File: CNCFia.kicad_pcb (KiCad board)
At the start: 2 copper layers, 128.3 x 96.5 mm, 89 parts, among them J1 GND, J10 Driver_X, J11 Driver_Y, J12 Driver_Z, J14 Spin_10V, J15 Relay_1, J16 Relay_2, J17 Relay_3, J2 EXT_5V, J3 Limit SW_XY, J4 Limit SW_ZA, J5 Extra SW 0, J6 Extra SW 1, J7 EXT_12V, J8 OPTO_5V, J9 Signal Input, Q1 BSS138, Q13 2N3904, Q14 2N3904, Q15 2N3904, Q2 BSS138, Q3 BSS138, Q4 BSS138, Q5 BSS138, Q6 BSS138, Q7 BSS138, Q8 BSS138, Q9 BSS138, U1 LTV-847, U2 LTV-847, U5 LM358P

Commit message: Before autorouting
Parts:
- renumbered REF** to M3-1, REF** to M3-2, REF** to M3-3, REF** to M3-4
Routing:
- net OPTO_5V: track 143.4 -> 142.4 mm

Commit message: Pre-SMD
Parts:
- moved M3-2 19.2 mm to (52.1, 100.2)
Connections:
- net LV_1 renamed X_Enbl
- net LV_2 renamed X_Dir
- net LV_3 renamed X_Step
- net LV_4 renamed Y_Enbl
- net LV_5 renamed Y_Dir
- net LV_6 renamed Y_Step
- net LV_7 renamed Z_Enbl
- net LV_8 renamed Z_Dir
- net LV_9 renamed Z_Step
- J1 pad 2: GND -> +5V
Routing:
- net GND: track 69.0 -> 195.1 mm, vias 1 -> 0
- net +5V: track 152.4 -> 235.4 mm
- net Probe: track 119.0 -> 53.7 mm
- net LIM_YMin: track 118.2 -> 63.8 mm
- net IN_Relay_1: track 112.0 -> 59.6 mm
- net Z_Dir: track 157.8 -> 105.8 mm, vias 1 -> 0
- net IN_Relay_2: track 120.5 -> 70.5 mm
- net Net-(D5-Pad2): track 136.1 -> 86.5 mm
- net Z_Step: track 157.0 -> 110.7 mm
- net X_Step: track 125.9 -> 82.0 mm, vias 0 -> 1
- net LIM_YMax: track 118.4 -> 75.2 mm
- net LIM_ZMax: track 95.9 -> 55.0 mm
- net Y_Dir: track 130.4 -> 90.2 mm, vias 1 -> 0
- net IN_Relay_3: track 117.4 -> 82.5 mm
- net LIM_XMax: track 93.6 -> 59.6 mm
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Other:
- board text added: "+12V GND"
- board text added: "+5V GND"
- board text added: "+5V OUT GND"
- board text added: "5V Source"
- board text added: "Controller Input"
- board text added: "Extra Probe Z Max Z Min"
- board text added: "GND E. Stop C. Start"
- board text added: "GND F. Hold Reset Door"
- board text added: "GND Spindle 0-10V"
- board text added: "NO COM NC Relay 2"
- board text added: "NO COM NC Relay 3"
- board text added: "Opto 5V GND"
- board text added: "Opto V Source"
- board text added: "X Step Dir Enable"
- board text added: "Y Max Y Min X Max X Min"
- board text added: "Y Step Dir Enable"
- board text added: "Z Step Dir Enable"
- board text added: "c6p.dev CNCFia b1"

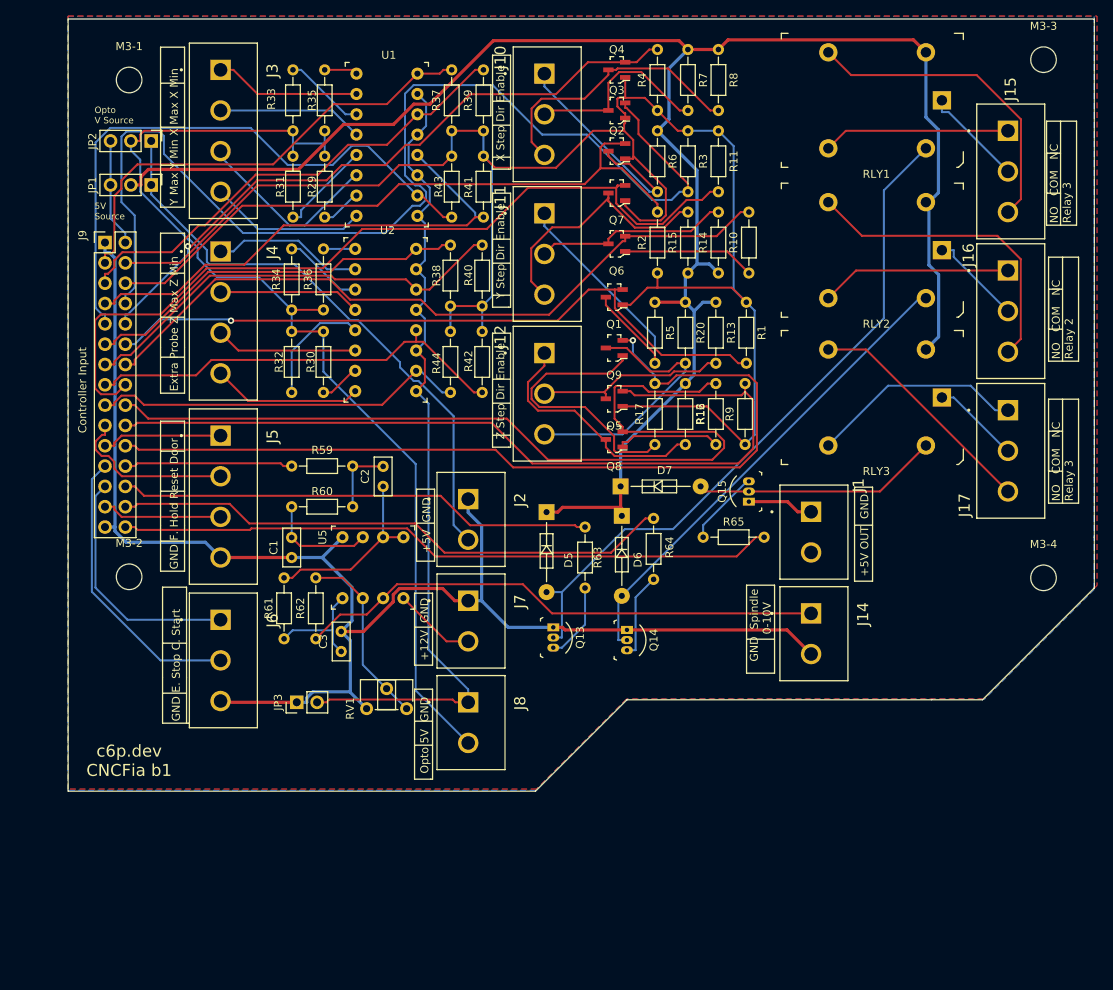
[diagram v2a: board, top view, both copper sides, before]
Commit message: Makes it SMD based, with smaller connectors
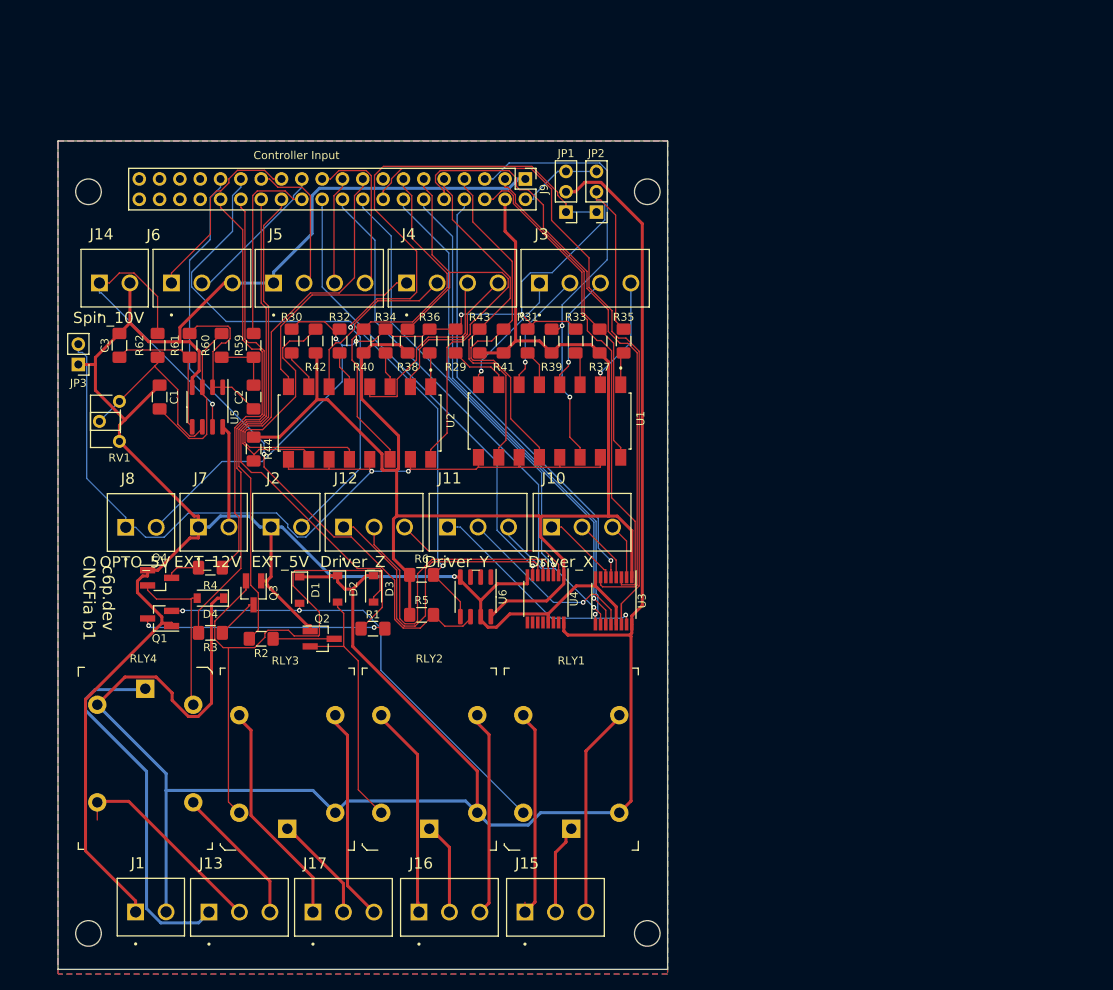
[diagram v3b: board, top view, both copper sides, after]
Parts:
- removed M3-1, M3-2, M3-3, M3-4: MountingHole_3.2mm_M3, MountingHole:MountingHole_3.2mm_M3
- removed Q13, Q14: 2N3904, digikey-footprints:TO-92-3
- removed the Q3 at (113.0, 41.9)
- removed Q5, Q6, Q7, Q8, Q9: BSS138, digikey-footprints:SOT-23-3
- removed R10, R11, R12, R13, R14, R15, R16, R17, R20, R7, R8, R9: 10k, Resistor_THT:R_Axial_DIN0204_L3.6mm_D1.6mm_P7.62mm_Horizontal
- removed R63, R64, R65: 2k2, Resistor_THT:R_Axial_DIN0204_L3.6mm_D1.6mm_P7.62mm_Horizontal
- added D4: 1N4148, Diode_SMD:D_SOD-123, F.Cu at (62.2, 102.9)
- added J13: Coolant, Kicad_extra_components:CUI_TBP02R2-381-03BE, F.Cu at (62.0, 142.1)
- added MH1: MountingHole_3.2mm_M3, MountingHole:MountingHole_3.2mm_M3, F.Cu at (116.8, 52.1)
- added MH2: MountingHole_3.2mm_M3, MountingHole:MountingHole_3.2mm_M3, F.Cu at (116.8, 144.8)
- added MH3: MountingHole_3.2mm_M3, MountingHole:MountingHole_3.2mm_M3, F.Cu at (47.0, 144.8)
- added MH4: MountingHole_3.2mm_M3, MountingHole:MountingHole_3.2mm_M3, F.Cu at (47.0, 52.1)
- added RLY4: G5LE-14_DC5, digikey-footprints:Relay_THT_G5LE-14, F.Cu at (54.1, 114.2)
- added U3: 4504, Package_SO:TSSOP-16_4.4x5mm_P0.65mm, F.Cu at (112.6, 103.2)
- added U4: 4504, Package_SO:TSSOP-16_4.4x5mm_P0.65mm, F.Cu at (104.1, 103.0)
- added U6: 24LC16, Package_SO:SOIC-8_3.9x4.9mm_P1.27mm, F.Cu at (95.4, 102.7)
- C1, C2, C3: footprint Kicad_extra_components:C_Rect_L4.6mm_W2.0mm_P2.50mm_MKS02_FKP02 -> Capacitor_SMD:C_1206_3216Metric_Pad1.42x1.75mm_HandSolder
- D1: renamed from D5; footprint digikey-footprints:Diode_DO-35_P10mm -> Diode_SMD:D_SOD-123
- D2: renamed from D6; footprint digikey-footprints:Diode_DO-35_P10mm -> Diode_SMD:D_SOD-123
- D3: renamed from D7; footprint digikey-footprints:Diode_DO-35_P10mm -> Diode_SMD:D_SOD-123
- J1, J14, J2, J7, J8: footprint Kicad_extra_components:CUI_TBP01R2-508-02BE -> Kicad_extra_components:CUI_TBP02R2-381-02BE
- J10, J11, J12, J6: footprint Kicad_extra_components:CUI_TBP01R2-508-03BE -> Kicad_extra_components:CUI_TBP02R2-381-03BE
- J15: value Relay_1 -> Spin_Enabl; footprint Kicad_extra_components:CUI_TBP01R2-508-03BE -> Kicad_extra_components:CUI_TBP02R2-381-03BE
- J16: value Relay_2 -> Spin_Dir; footprint Kicad_extra_components:CUI_TBP01R2-508-03BE -> Kicad_extra_components:CUI_TBP02R2-381-03BE
- J17: value Relay_3 -> Mist; footprint Kicad_extra_components:CUI_TBP01R2-508-03BE -> Kicad_extra_components:CUI_TBP02R2-381-03BE
- J3, J4, J5: footprint Kicad_extra_components:CUI_TBP01R2-508-04BE -> Kicad_extra_components:CUI_TBP02R2-381-04BE
- J9: footprint Connector_PinHeader_2.54mm:PinHeader_2x15_P2.54mm_Vertical -> Connector_PinHeader_2.54mm:PinHeader_2x20_P2.54mm_Vertical
- Q1, Q2, Q4: value BSS138 -> 2N3904; footprint digikey-footprints:SOT-23-3 -> Package_TO_SOT_SMD:SOT-23_Handsoldering
- Q3: renamed from Q15; footprint digikey-footprints:TO-92-3 -> Package_TO_SOT_SMD:SOT-23_Handsoldering
- R1, R2, R3, R4, R5, R6: value 10k -> 2k2; footprint Resistor_THT:R_Axial_DIN0204_L3.6mm_D1.6mm_P7.62mm_Horizontal -> Resistor_SMD:R_1206_3216Metric_Pad1.42x1.75mm_HandSolder
- R29, R30, R31, R32, R33, R34, R35, R36, R37, R38, R39, R40, R41, R42, R43, R44, R59, R60, R61, R62: footprint Resistor_THT:R_Axial_DIN0204_L3.6mm_D1.6mm_P7.62mm_Horizontal -> Resistor_SMD:R_1206_3216Metric_Pad1.42x1.75mm_HandSolder
- U1, U2: footprint digikey-footprints:Socket_DIP-16_7.62mm_Conn -> Kicad_extra_components:SOIC254P1016X460-16N
- U5: footprint digikey-footprints:SOCKET_DIP-8_7.62mm_Conn -> Package_SO:SOIC-8_3.9x4.9mm_P1.27mm
- moved J15 114.8 mm to (101.5, 142.1), turned to 0 degrees
- moved J16 108.9 mm to (88.3, 142.1), turned to 0 degrees
- moved J17 107.2 mm to (75.0, 142.1), turned to 0 degrees
- moved RLY1 102.2 mm to (107.3, 131.7), turned to 90 degrees
- moved J1 98.1 mm to (52.9, 142.1), turned to 0 degrees
- moved J14 98.1 mm to (48.4, 63.5), turned to 0 degrees
- moved RLY3 98.0 mm to (71.8, 131.7), turned to 90 degrees
- moved RLY2 96.6 mm to (89.6, 131.7), turned to 90 degrees
- moved R3 86.6 mm to (62.2, 107.2), turned to 180 degrees
- moved Q4 85.4 mm to (55.9, 100.3), turned to 0 degrees
- moved R4 79.9 mm to (62.2, 99.1), turned to 0 degrees
- moved Q2 71.2 mm to (76.2, 108.0), turned to 0 degrees
- moved Q1 69.6 mm to (55.9, 105.4)
- moved R2 67.4 mm to (68.6, 108.0), turned to 180 degrees
- moved Q3 63.0 mm to (67.6, 102.2), turned to -90 degrees
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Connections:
- net /PWM to V converter/OUT_Spn_10V_0 renamed /OUT_Spn_10V_0
- net /Relays/Relay_COM_1 renamed /Relay_COM_1
- net /Relays/Relay_COM_2 renamed /Relay_COM_2
- net /Relays/Relay_COM_3 renamed /Relay_COM_3
- net /Relays/Relay_NC_1 renamed /Relay_NC_1
- net /Relays/Relay_NC_2 renamed /Relay_NC_2
- net /Relays/Relay_NC_3 renamed /Relay_NC_3
- net /Relays/Relay_NO_1 renamed /Relay_NO_1
- net /Relays/Relay_NO_2 renamed /Relay_NO_2
- net /Relays/Relay_NO_3 renamed /Relay_NO_3
- net SPIN_PWM renamed Spin_PWM
- D1 pad 2: Net-(D5-Pad2) -> Net-(D1-Pad2)
- D2 pad 2: Net-(D6-Pad2) -> Net-(D2-Pad2)
- J10 pad 1: /Level Shifters/HV_1 -> /HV_3
- J10 pad 2: /Level Shifters/HV_2 -> /HV_2
- J10 pad 3: /Level Shifters/HV_3 -> /HV_1
- J11 pad 1: /Level Shifters/HV_4 -> /HV_6
- J11 pad 2: /Level Shifters/HV_5 -> /HV_5
- J11 pad 3: /Level Shifters/HV_6 -> /HV_4
- J12 pad 1: /Level Shifters/HV_7 -> /HV_9
- J12 pad 2: /Level Shifters/HV_8 -> /HV_8
- J12 pad 3: /Level Shifters/HV_9 -> /HV_7
- J3 pad 1: /Opto-isolated switches/SW_XMIN -> /SW_YMAX
- J3 pad 2: /Opto-isolated switches/SW_XMAX -> /SW_YMIN
- J3 pad 3: /Opto-isolated switches/SW_YMIN -> /SW_XMAX
- J3 pad 4: /Opto-isolated switches/SW_YMAX -> /SW_XMIN
- J4 pad 1: /Opto-isolated switches/SW_ZMIN -> /SW_Extra
- J4 pad 2: /Opto-isolated switches/SW_ZMAX -> /SW_Probe
- J4 pad 3: /Opto-isolated switches/SW_Probe -> /SW_ZMAX
- J4 pad 4: /Opto-isolated switches/SW_Extra -> /SW_ZMIN
- J5 pad 1: Door -> GND
- J5 pad 2: Reset -> Feed_Hold
- J5 pad 3: Feed_Hold -> Reset
- J5 pad 4: GND -> Door
- J9 pad 26: IN_Relay_1 -> Spin_Enbl
- J9 pad 28: IN_Relay_2 -> Spin_Dir
- J9 pad 29: GND -> E_SDA
- J9 pad 30: IN_Relay_3 -> Mist
- Q1 pad 1: +3V3 -> GND
- Q1 pad 2: Y_Enbl -> Net-(D1-Pad2)
- Q1 pad 3: /Level Shifters/HV_4 -> Net-(Q1-Pad3)
- Q2 pad 1: +3V3 -> GND
- Q2 pad 2: X_Enbl -> Net-(D2-Pad2)
- Q2 pad 3: /Level Shifters/HV_1 -> Net-(Q2-Pad3)
- Q3 pad 3: Net-(Q15-Pad3) -> Net-(Q3-Pad3)
- Q4 pad 1: +3V3 -> GND
- Q4 pad 2: X_Step -> Net-(D4-Pad2)
- Q4 pad 3: /Level Shifters/HV_3 -> Net-(Q4-Pad3)
- R1 pad 1: +3V3 -> Net-(Q1-Pad3)
- R1 pad 2: Y_Enbl -> Spin_Enbl
- R2 pad 1: +3V3 -> Net-(Q2-Pad3)
- R2 pad 2: X_Enbl -> Spin_Dir
- R3 pad 1: +3V3 -> Net-(Q3-Pad3)
- R3 pad 2: X_Dir -> Mist
- R4 pad 1: +3V3 -> Net-(Q4-Pad3)
- R4 pad 2: X_Step -> Flood
- R42 pad 2: Probe -> /Opto-isolated switches/e
- R5 pad 1: +5V -> +3V3
- R5 pad 2: /Level Shifters/HV_4 -> E_SCL
- R6 pad 1: +5V -> +3V3
- R6 pad 2: /Level Shifters/HV_1 -> E_SDA
- RLY1 pad 5: Net-(D5-Pad2) -> Net-(D1-Pad2)
- RLY2 pad 5: Net-(D6-Pad2) -> Net-(D2-Pad2)
- U1 pad 2: /Opto-isolated switches/SW_XMIN -> /SW_XMIN
- U1 pad 4: /Opto-isolated switches/SW_XMAX -> /SW_XMAX
- U1 pad 6: /Opto-isolated switches/SW_YMIN -> /SW_YMIN
- U1 pad 8: /Opto-isolated switches/SW_YMAX -> /SW_YMAX
- U2 pad 12: Probe -> /Opto-isolated switches/e
- U2 pad 2: /Opto-isolated switches/SW_ZMIN -> /SW_ZMIN
- U2 pad 4: /Opto-isolated switches/SW_ZMAX -> /SW_ZMAX
- U2 pad 6: /Opto-isolated switches/SW_Probe -> /SW_Probe
- U2 pad 8: /Opto-isolated switches/SW_Extra -> /SW_Extra
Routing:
- net Net-(D5-Pad2): track 86.5 -> 0.00 mm
- net X_Dir: track 140.2 -> 55.6 mm, vias 0 -> 1
- net IN_Relay_3: track 82.5 -> 0.00 mm
- net E_SDA: track 0.00 -> 81.3 mm, vias 0 -> 1
- net E_SCL: track 0.00 -> 80.4 mm, vias 0 -> 1
- net GND: track 195.1 -> 272.5 mm, vias 0 -> 1
- net IN_Relay_2: track 70.5 -> 0.00 mm
- net Spin_Enbl: track 0.00 -> 68.1 mm
- net Mist: track 0.00 -> 60.8 mm
- net Net-(D6-Pad2): track 60.2 -> 0.00 mm
- net IN_Relay_1: track 59.6 -> 0.00 mm
- net Spin_Dir: track 0.00 -> 59.1 mm
- net Net-(D1-Pad2): track 0.00 -> 58.4 mm, vias 0 -> 2
- net Z_Enbl: track 111.7 -> 56.9 mm, vias 0 -> 1
- net Probe: track 53.7 -> 0.00 mm
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- added copper zone on F.Cu, net +3V3
- removed copper zone on F.Cu, net +5V
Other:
- board size 128.3 x 96.5 mm -> 76.2 x 103.6 mm
- net class Default: clearance 0.2 -> 0.127; trace_width 0.25 -> 0.127; via_dia 0.8 -> 0.6; via_drill 0.4 -> 0.3
- rule trace_clearance: 0.2 -> 0.127
- rule trace_min: 0.2 -> 0.127
- rule via_min_size: 0.4 -> 0.6
- board text removed: "+12V GND"
- board text removed: "+5V GND"
- board text removed: "+5V OUT GND"
- board text removed: "5V Source"
- board text removed: "Extra Probe Z Max Z Min"
- board text removed: "GND E. Stop C. Start"
- board text removed: "GND F. Hold Reset Door"
- board text removed: "GND Spindle 0-10V"
- board text removed: "NO COM NC Relay 2"
- board text removed: "NO COM NC Relay 3"
- board text removed: "Opto 5V GND"
- board text removed: "Opto V Source"
- board text removed: "X Step Dir Enable"
- board text removed: "Y Max Y Min X Max X Min"
- board text removed: "Y Step Dir Enable"
- board text removed: "Z Step Dir Enable"

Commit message: Vertical mounted version
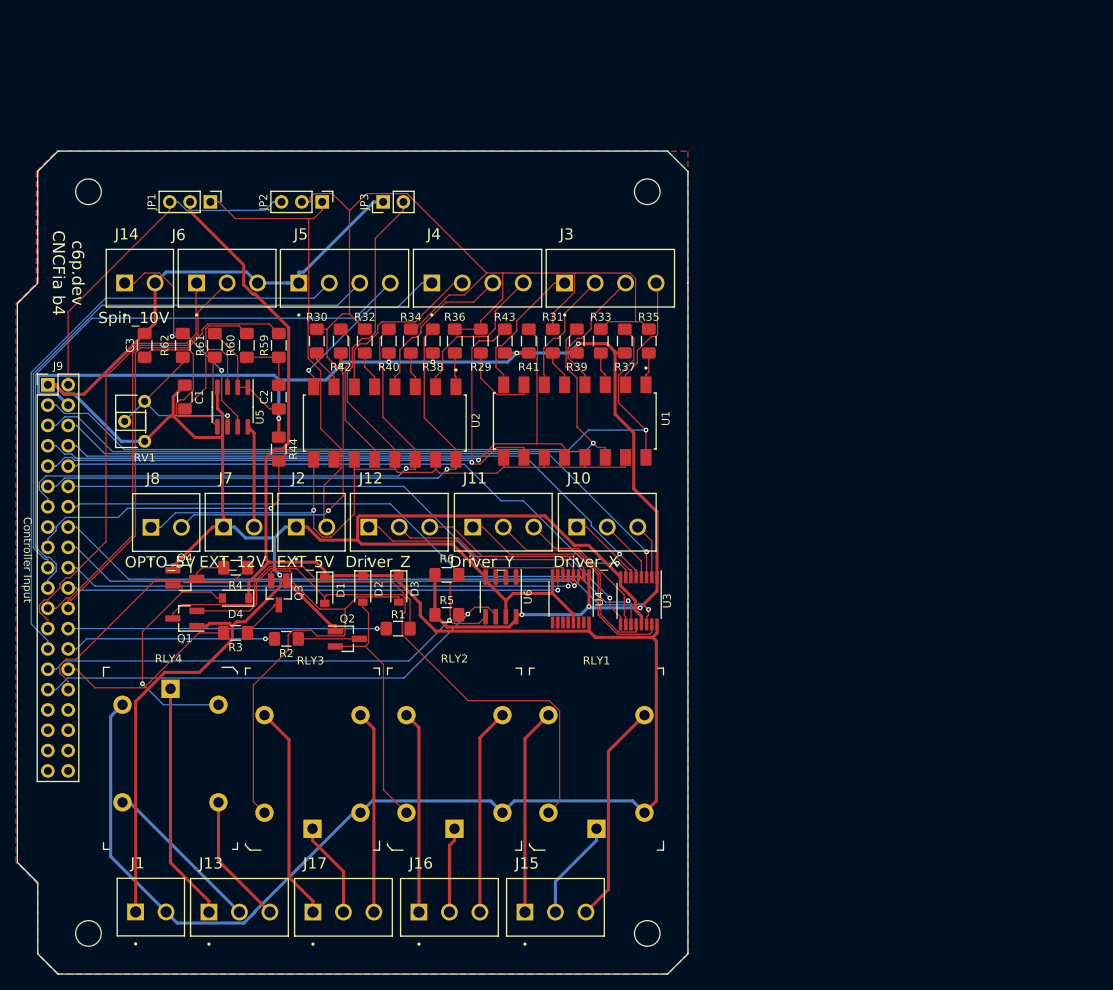
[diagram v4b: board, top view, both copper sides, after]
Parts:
- moved J9 65.0 mm to (41.9, 76.2), turned to 0 degrees
- moved JP1 44.5 mm to (62.2, 53.3), turned to -90 degrees
- moved JP3 43.2 mm to (83.8, 53.3), turned to 90 degrees
- moved JP2 34.3 mm to (76.2, 53.3), turned to -90 degrees
- moved C2 3.15 mm to (70.8, 77.7)
- moved D1 3.15 mm to (76.5, 101.9)
- moved D2 3.15 mm to (81.3, 101.7)
- moved D3 3.15 mm to (85.8, 101.7)
- moved J10 3.15 mm to (108.0, 94.0)
- moved J11 3.15 mm to (95.0, 94.0)
- moved J12 3.15 mm to (82.0, 94.0)
- moved J3 3.15 mm to (106.5, 63.5)
- moved J5 3.15 mm to (73.3, 63.5)
- moved Q3 3.15 mm to (70.8, 102.2)
- moved R1 3.15 mm to (85.7, 106.7)
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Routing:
- net Feed_Hold: track 18.3 -> 77.3 mm
- net Reset: track 13.5 -> 70.7 mm
- net Door: track 20.6 -> 77.5 mm
- net LIM_XMin: track 41.0 -> 96.8 mm, vias 0 -> 1
- net LIM_YMax: track 44.1 -> 81.8 mm, vias 0 -> 1
- net Mist: track 60.8 -> 23.2 mm
- net OPTO_5V: track 119.3 -> 156.7 mm, vias 4 -> 1
- net LIM_YMin: track 45.5 -> 82.4 mm, vias 0 -> 1
- net E_Stop: track 18.7 -> 54.3 mm
- net LIM_XMax: track 57.2 -> 90.0 mm, vias 2 -> 1
- net Spin_Dir: track 59.1 -> 26.3 mm, vias 0 -> 1
- net Cycle_Start: track 23.8 -> 55.8 mm
- net Spin_PWM: track 24.1 -> 55.9 mm
- net MCU_5V: track 11.7 -> 43.0 mm
- net +5V: track 265.1 -> 235.1 mm
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- added copper zone on B.Cu, net +3V3
- added copper zone on F.Cu, net GND
- removed copper zone on F.Cu, net +3V3
- removed copper zone on B.Cu, net GND
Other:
- board size 76.2 x 103.6 mm -> 83.8 x 102.9 mm
- net class Power added: clearance 0.127, trace_width 0.381, via_dia 0.6, via_drill 0.3
- board text added: "c6p.dev CNCFia b4"
- board text removed: "c6p.dev CNCFia b1"

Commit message: New routing
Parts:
- moved RLY4 17.4 mm to (57.3, 131.6), turned to 90 degrees
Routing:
- net /Relay_NC_4: track 16.4 -> 42.5 mm
- net /Relay_COM_4: track 29.9 -> 12.6 mm
- net +5V: track 235.1 -> 219.1 mm
- net Net-(D4-Pad2): track 31.4 -> 40.1 mm
- net /Relay_NO_4: track 20.3 -> 26.8 mm
- net /SW_Probe: track 22.1 -> 21.1 mm
- net +3V3: track 169.1 -> 168.4 mm
- net OPTO_5V: track 156.7 -> 156.2 mm
- net EXT_5V: track 57.6 -> 57.1 mm
